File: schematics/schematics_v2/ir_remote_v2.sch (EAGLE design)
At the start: 24 parts, among them IC2 7805T, T11 TASTER3301, T12 TASTER3301, T13 TASTER3301, T14 TASTER3301, T15 TASTER3301

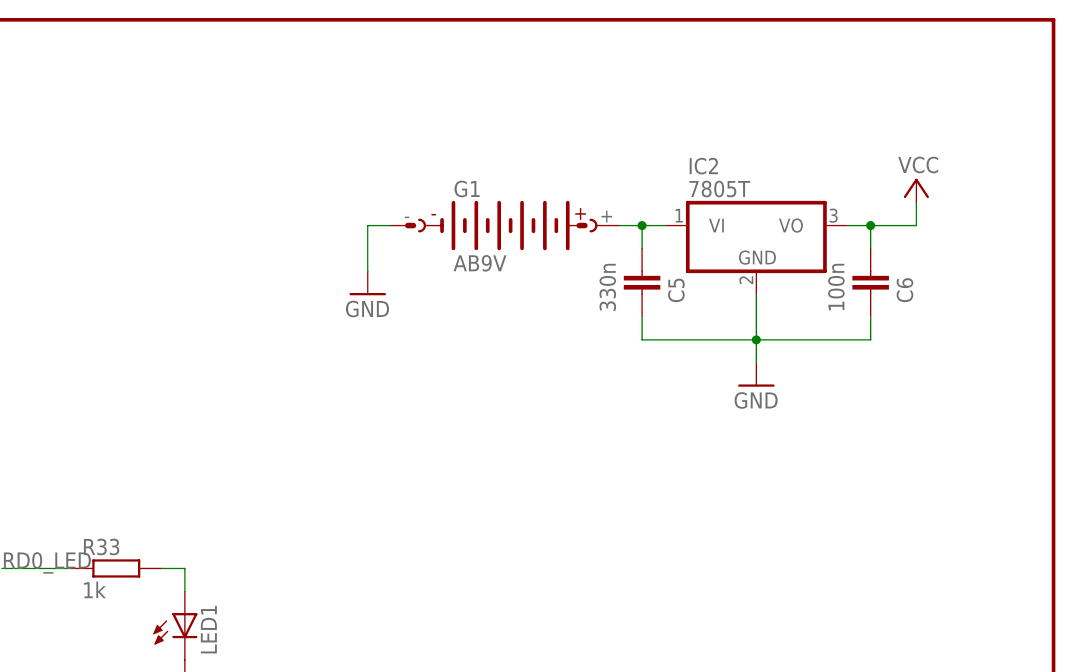
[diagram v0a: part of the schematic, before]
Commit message: Modify power supply with AP1117E50G replacing LM7805
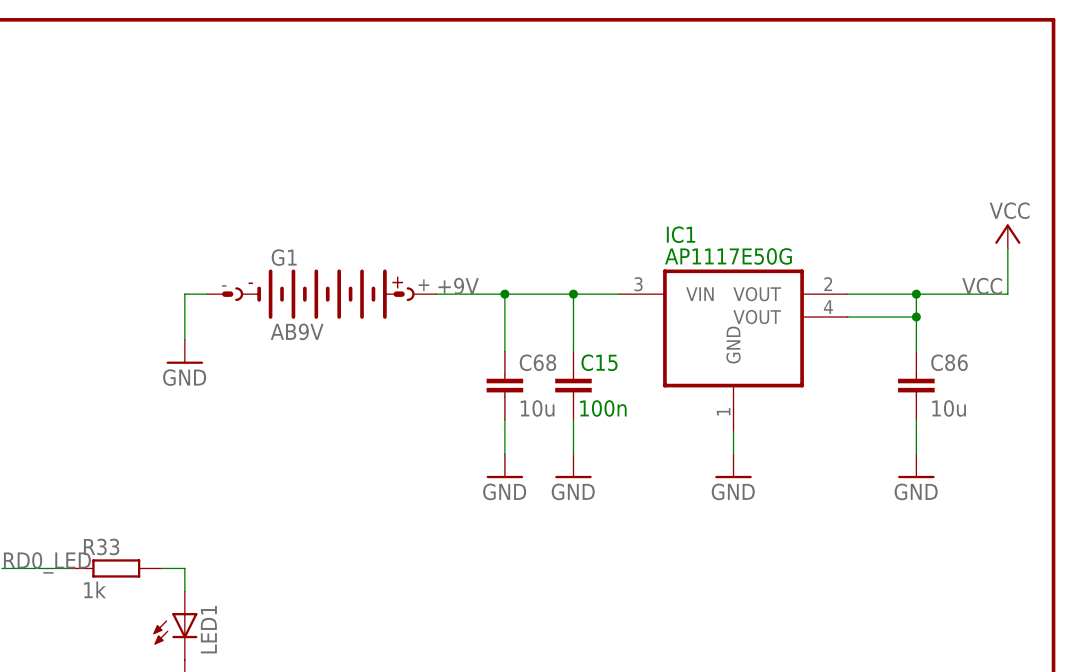
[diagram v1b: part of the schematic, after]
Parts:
- removed C5: 330n, rcl:C-EUC0805
- removed C6: 100n, rcl:C-EUC0805
- removed IC2: 7805T, linear:7805T
- added C15: 100n, rcl_416:C-EUC0805
- added C68, C86: 10u, rcl:C-EUC0805
- added IC1: AP1117E50G, Bernd_110428:REG1117-2OUT
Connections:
- removed net N$34: C5.1, G1.+, IC2.VI
- new net +9V: C15.1, C68.1, G1.+, IC1.VIN
- net GND: now also C15.2, C68.2, C86.2, IC1.GND; no longer C5.2, C6.2, IC2.GND
- net VCC: now also C86.1, IC1.VOUT, IC1.VOUT@1; no longer C6.1, IC2.VO
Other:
- moved on the sheet: G1
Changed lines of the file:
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@@
 <part name="GND30" library="supply1" deviceset="GND" device=""/>
 <part name="G1" library="battery" deviceset="AB9V" device=""/>
-<part name="IC2" library="linear" deviceset="78*" device="T" technology="05"/>
-<part name="C5" library="rcl" deviceset="C-EU" device="C0805" value="330n"/>
-<part name="C6" library="rcl" deviceset="C-EU" device="C0805" value="100n"/>
 <part name="GND2" library="supply1" deviceset="GND" device=""/>
-<part name="GND6" library="supply1" deviceset="GND" device=""/>
-<part name="P+6" library="supply1" deviceset="VCC" device=""/>
 <part name="C11" library="rcl" deviceset="C-EU" device="C0805" value="18p"/>
+<part name="C15" library="rcl_416" deviceset="C-EU" device="C0805" value="100n"/>
+<part name="GND25" library="supply1" deviceset="GND" device=""/>
+<part name="GND85" library="supply1" deviceset="GND" device=""/>
+<part name="C68" library="rcl" deviceset="C-EU" device="C0805" value="10u"/>
+<part name="GND90" library="supply1" deviceset="GND" device=""/>
+<part name="GND91" library="supply1" deviceset="GND" device=""/>
+<part name="C86" library="rcl" deviceset="C-EU" device="C0805" value="10u"/>
+<part name="IC1" library="Bernd_110428" deviceset="REG1117-2OUT" device="" value="AP1117E50G"/>
+<part name="P+1" library="supply1" deviceset="VCC" device=""/>
 </parts>
 <sheets>
@@
 <instance part="LED1" gate="G$1" x="167.64" y="114.3"/>
 <instance part="GND30" gate="1" x="167.64" y="106.68"/>
-<instance part="G1" gate="G$1" x="203.2" y="157.48"/>
-<instance part="IC2" gate="A1" x="231.14" y="157.48"/>
-<instance part="C5" gate="G$1" x="218.44" y="152.4" smashed="yes">
-<attribute name="NAME" x="223.139" y="148.844" size="1.778" layer="95" rot="R90"/>
-<attribute name="VALUE" x="213.741" y="153.416" size="1.778" layer="96" rot="R270"/>
-</instance>
-<instance part="C6" gate="G$1" x="243.84" y="152.4" smashed="yes">
-<attribute name="NAME" x="248.539" y="148.844" size="1.778" layer="95" rot="R90"/>
-<attribute name="VALUE" x="239.141" y="153.416" size="1.778" layer="96" rot="R270"/>
-</instance>
-<instance part="GND2" gate="1" x="187.96" y="149.86"/>
-<instance part="GND6" gate="1" x="231.14" y="139.7"/>
-<instance part="P+6" gate="VCC" x="248.92" y="162.56" smashed="yes">
-<attribute name="VALUE" x="251.46" y="165.1" size="1.778" layer="96" rot="R180"/>
-</instance>
+<instance part="G1" gate="G$1" x="182.88" y="149.86"/>
+<instance part="GND2" gate="1" x="167.64" y="142.24"/>
 <instance part="C11" gate="G$1" x="66.04" y="129.54" smashed="yes" rot="MR90">
 <attribute name="NAME" x="59.944" y="131.699" size="1.778" layer="95" rot="MR180"/>
 <attribute name="VALUE" x="59.944" y="129.159" size="1.778" layer="96" rot="MR180"/>
+</instance>
+<instance part="C15" gate="G$1" x="210.82" y="140.97" smashed="yes">
+<attribute name="NAME" x="211.582" y="141.351" size="1.778" layer="91"/>
+<attribute name="VALUE" x="211.328" y="136.271" size="1.778" layer="91"/>
+</instance>
+<instance part="GND25" gate="1" x="210.82" y="129.54"/>
+<instance part="GND85" gate="1" x="228.6" y="129.54"/>
+<instance part="C68" gate="G$1" x="203.2" y="140.97"/>
+<instance part="GND90" gate="1" x="203.2" y="129.54"/>
+<instance part="GND91" gate="1" x="248.92" y="129.54"/>
+<instance part="C86" gate="G$1" x="248.92" y="140.97"/>
+<instance part="IC1" gate="G$1" x="228.6" y="147.32" smashed="yes">
+<attribute name="NAME" x="220.98" y="155.575" size="1.778" layer="91" ratio="10"/>
+<attribute name="VALUE" x="220.98" y="153.162" size="1.778" layer="91" ratio="10"/>
+</instance>
+<instance part="P+1" gate="VCC" x="259.08" y="157.48" smashed="yes">
+<attribute name="VALUE" x="261.62" y="160.02" size="1.778" layer="96" rot="R180"/>
 </instance>
 </instances>
@@
 <segment>
 <pinref part="G1" gate="G$1" pin="-"/>
-<wire x1="190.5" y1="157.48" x2="187.96" y2="157.48" width="0.1524" layer="91"/>
-<wire x1="187.96" y1="157.48" x2="187.96" y2="152.4" width="0.1524" layer="91"/>
+<wire x1="170.18" y1="149.86" x2="167.64" y2="149.86" width="0.1524" layer="91"/>
+<wire x1="167.64" y1="149.86" x2="167.64" y2="144.78" width="0.1524" layer="91"/>
 <pinref part="GND2" gate="1" pin="GND"/>
 </segment>
 <segment>
-<pinref part="C5" gate="G$1" pin="2"/>
-<wire x1="218.44" y1="147.32" x2="218.44" y2="144.78" width="0.1524" layer="91"/>
-<wire x1="218.44" y1="144.78" x2="231.14" y2="144.78" width="0.1524" layer="91"/>
-<pinref part="IC2" gate="A1" pin="GND"/>
-<wire x1="231.14" y1="144.78" x2="231.14" y2="149.86" width="0.1524" layer="91"/>
-<pinref part="C6" gate="G$1" pin="2"/>
-<wire x1="243.84" y1="147.32" x2="243.84" y2="144.78" width="0.1524" layer="91"/>
-<wire x1="231.14" y1="144.78" x2="243.84" y2="144.78" width="0.1524" layer="91"/>
-<wire x1="231.14" y1="144.78" x2="231.14" y2="142.24" width="0.1524" layer="91"/>
-<pinref part="GND6" gate="1" pin="GND"/>
-<junction x="231.14" y="144.78"/>
+<wire x1="210.82" y1="135.89" x2="210.82" y2="132.08" width="0.1524" layer="91"/>
+<pinref part="C15" gate="G$1" pin="2"/>
+<pinref part="GND25" gate="1" pin="GND"/>
+</segment>
+<segment>
+<pinref part="GND85" gate="1" pin="GND"/>
+<pinref part="IC1" gate="G$1" pin="GND"/>
+<wire x1="228.6" y1="132.08" x2="228.6" y2="134.62" width="0.1524" layer="91"/>
+</segment>
+<segment>
+<wire x1="203.2" y1="132.08" x2="203.2" y2="135.89" width="0.1524" layer="91"/>
+<pinref part="C68" gate="G$1" pin="2"/>
+<pinref part="GND90" gate="1" pin="GND"/>
+</segment>
+<segment>
+<wire x1="248.92" y1="135.89" x2="248.92" y2="132.08" width="0.1524" layer="91"/>
+<pinref part="C86" gate="G$1" pin="2"/>
+<pinref part="GND91" gate="1" pin="GND"/>
 </segment>
 </net>
@@
 </segment>
 <segment>
-<pinref part="IC2" gate="A1" pin="VO"/>
-<wire x1="241.3" y1="157.48" x2="243.84" y2="157.48" width="0.1524" layer="91"/>
-<pinref part="C6" gate="G$1" pin="1"/>
-<wire x1="243.84" y1="157.48" x2="243.84" y2="154.94" width="0.1524" layer="91"/>
-<wire x1="243.84" y1="157.48" x2="248.92" y2="157.48" width="0.1524" layer="91"/>
-<wire x1="248.92" y1="157.48" x2="248.92" y2="160.02" width="0.1524" layer="91"/>
-<pinref part="P+6" gate="VCC" pin="VCC"/>
-<junction x="243.84" y="157.48"/>
+<wire x1="248.92" y1="149.86" x2="241.3" y2="149.86" width="0.1524" layer="91"/>
+<wire x1="248.92" y1="149.86" x2="248.92" y2="147.32" width="0.1524" layer="91"/>
+<wire x1="248.92" y1="147.32" x2="248.92" y2="143.51" width="0.1524" layer="91"/>
+<wire x1="241.3" y1="147.32" x2="248.92" y2="147.32" width="0.1524" layer="91"/>
+<junction x="248.92" y="147.32"/>
+<pinref part="C86" gate="G$1" pin="1"/>
+<pinref part="IC1" gate="G$1" pin="VOUT"/>
+<pinref part="IC1" gate="G$1" pin="VOUT@1"/>
+<wire x1="248.92" y1="149.86" x2="259.08" y2="149.86" width="0.1524" layer="91"/>
+<junction x="248.92" y="149.86"/>
+<label x="254" y="149.86" size="1.778" layer="95"/>
+<pinref part="P+1" gate="VCC" pin="VCC"/>
+<wire x1="259.08" y1="149.86" x2="259.08" y2="154.94" width="0.1524" layer="91"/>
 </segment>
 </net>
@@
 </segment>
 </net>
-<net name="N$34" class="0">
-<segment>
-<pinref part="G1" gate="G$1" pin="+"/>
-<pinref part="IC2" gate="A1" pin="VI"/>
-<wire x1="215.9" y1="157.48" x2="218.44" y2="157.48" width="0.1524" layer="91"/>
-<pinref part="C5" gate="G$1" pin="1"/>
-<wire x1="218.44" y1="157.48" x2="220.98" y2="157.48" width="0.1524" layer="91"/>
-<wire x1="218.44" y1="154.94" x2="218.44" y2="157.48" width="0.1524" layer="91"/>
-<junction x="218.44" y="157.48"/>
-</segment>
-</net>
 <net name="N$9" class="0">
 <segment>
@@
 </segment>
 </net>
+<net name="+9V" class="0">
+<segment>
+<wire x1="215.9" y1="149.86" x2="210.82" y2="149.86" width="0.1524" layer="91"/>
+<wire x1="203.2" y1="143.51" x2="203.2" y2="149.86" width="0.1524" layer="91"/>
+<wire x1="210.82" y1="143.51" x2="210.82" y2="149.86" width="0.1524" layer="91"/>
+<pinref part="C68" gate="G$1" pin="1"/>
+<pinref part="IC1" gate="G$1" pin="VIN"/>
+<pinref part="C15" gate="G$1" pin="1"/>
+<junction x="210.82" y="149.86"/>
+<wire x1="203.2" y1="149.86" x2="210.82" y2="149.86" width="0.1524" layer="91"/>
+<label x="195.58" y="149.86" size="1.778" layer="95"/>
+<pinref part="G1" gate="G$1" pin="+"/>
+<wire x1="195.58" y1="149.86" x2="203.2" y2="149.86" width="0.1524" layer="91"/>
+<junction x="203.2" y="149.86"/>
+</segment>
+</net>

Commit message: Clean up files in schematics v2
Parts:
- removed C11, C30: 18p, rcl:C-EUC0805
- removed Q4: (no value), crystal:CRYTALHC49U-V
- added C63, C66: 22p, rcl:C-EUC0603_WE
- added Q5: 10MHz, Bernd:XTAL_HC5032
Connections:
- removed net N$25: C11.1, IC8.OSC2/CLKOUT, Q4.1
- removed net N$9: C30.1, IC8.OSC1/CLKIN, Q4.2
- new net N$47: C66.2, IC8.OSC1/CLKIN, Q5.1
- new net N$48: C63.2, IC8.OSC2/CLKOUT, Q5.2
- net GND: now also C63.1, C66.1; no longer C11.2, C30.2
